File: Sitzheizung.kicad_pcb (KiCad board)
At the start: 2 copper layers, 1 part, among them Q1 BUK9M9R1-40EX

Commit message: finished layout
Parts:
- added C1: 100n, Capacitor_SMD:C_0805_2012Metric_Pad1.15x1.40mm_HandSolder, F.Cu at (163.5, 102.8)
- added C2: 10u, Capacitor_THT:CP_Radial_D8.0mm_P5.00mm, F.Cu at (146.5, 113.8)
- added C3: 100n, Capacitor_SMD:C_0805_2012Metric_Pad1.15x1.40mm_HandSolder, F.Cu at (156.1, 97.6)
- added C4: 1u, Capacitor_THT:CP_Radial_D8.0mm_P5.00mm, F.Cu at (156.2, 109.8)
- added D1: D, Diode_SMD:D_MiniMELF, F.Cu at (145.2, 97.7)
- added D2: LED, LED_SMD:LED_0805_2012Metric_Pad0.98x1.40mm_HandSolder, F.Cu at (154.7, 92.8)
- added J1: Conn_01x06_Male, Connector_TE-Connectivity:TE_MQS_936287-2_1x06_P2.54mm_Horizontal, F.Cu at (139.9, 98.0)
- added R1: 650R, Resistor_SMD:R_0805_2012Metric_Pad1.15x1.40mm_HandSolder, F.Cu at (157.2, 92.8)
- added R2: R, Resistor_SMD:R_0805_2012Metric_Pad1.15x1.40mm_HandSolder, F.Cu at (151.5, 97.6)
- added R3: 1k, Resistor_SMD:R_0805_2012Metric_Pad1.15x1.40mm_HandSolder, F.Cu at (150.3, 109.0)
- added R4: 15k, Resistor_SMD:R_0805_2012Metric_Pad1.15x1.40mm_HandSolder, F.Cu at (149.7, 102.9)
- added R5: 1k8, Resistor_SMD:R_0805_2012Metric_Pad1.15x1.40mm_HandSolder, F.Cu at (160.9, 97.7)
- added R6: 1k, Resistor_SMD:R_0805_2012Metric_Pad1.15x1.40mm_HandSolder, F.Cu at (161.8, 108.5)
- added RV1: 15k, Potentiometer_THT:Potentiometer_Bourns_3386X_Horizontal, F.Cu at (145.2, 94.3)
- added U1: TL494, Package_SO:SOIC-16_3.9x9.9mm_P1.27mm, F.Cu at (156.6, 102.8)
- moved Q1 107.8 mm to (144.9, 103.8), turned to 90 degrees
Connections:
- Q1 pad 4: (no net) -> Net-(Q1-Pad4)
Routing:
- net Net-(C1-Pad1): track 0.00 -> 41.9 mm, vias 0 -> 3
- net Poti_1: track 0.00 -> 38.3 mm, vias 0 -> 2
- net KL31: track 0.00 -> 32.1 mm, vias 0 -> 7
- net Heizung+: track 0.00 -> 27.0 mm, vias 0 -> 1
- net Heizung-: track 0.00 -> 19.1 mm, vias 0 -> 7
- net Net-(R2-Pad1): track 0.00 -> 18.2 mm, vias 0 -> 2
- net Net-(R4-Pad2): track 0.00 -> 17.7 mm
- net Net-(R3-Pad1): track 0.00 -> 6.64 mm
- net Net-(R3-Pad2): track 0.00 -> 5.81 mm
- net Net-(C4-Pad1): track 0.00 -> 4.64 mm
- net Net-(Q1-Pad4): track 0.00 -> 4.62 mm
- net Net-(R6-Pad1): track 0.00 -> 4.29 mm
- net Net-(D2-Pad2): track 0.00 -> 2.61 mm
- added copper zone on B.Cu, net Heizung-
- added copper zone on F.Cu, net Heizung-
- added copper zone on B.Cu, net KL31
- added copper zone on F.Cu, net KL31
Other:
- board outline added: 34 x 34 mm
- net class Default: clearance 0.2 -> 0.15
- rule trace_clearance: 0.2 -> 0.15
- rule trace_min: 0.2 -> 0.15
- board text added: "Auxilary Heater"
- board text added: "v1.0"

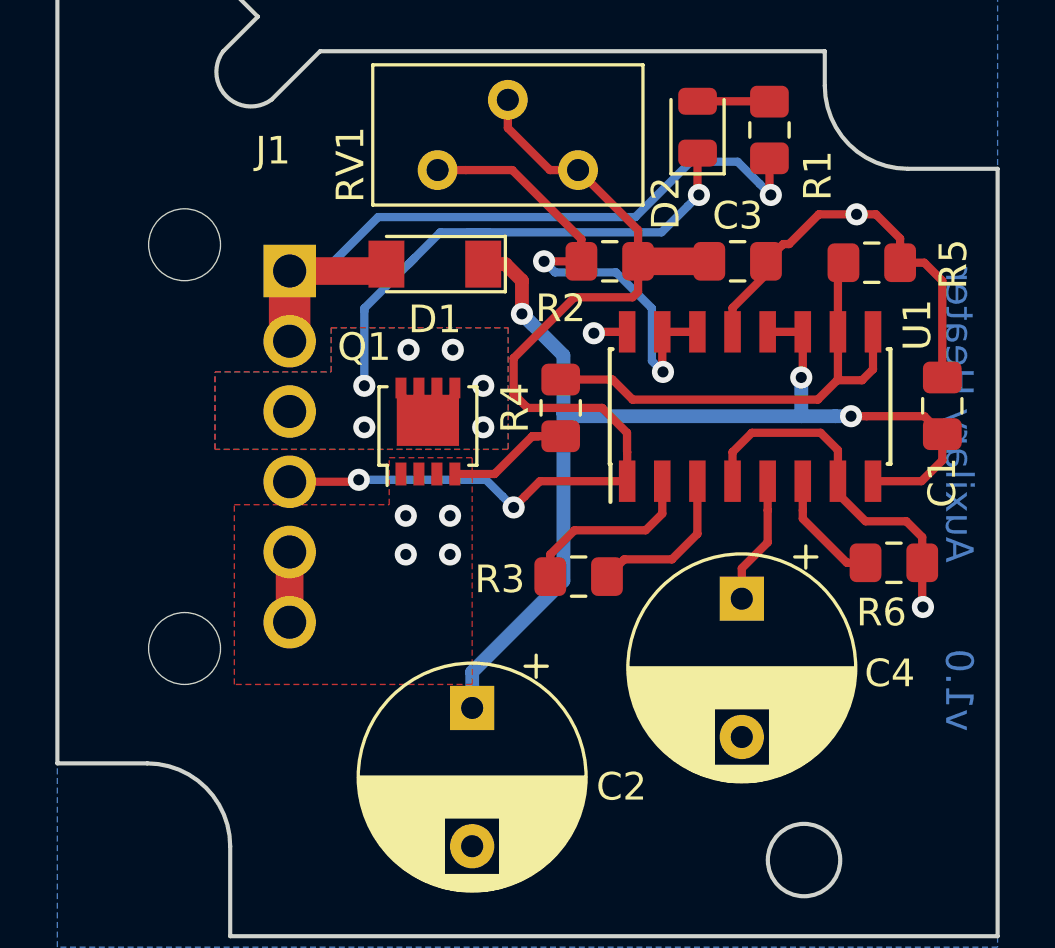
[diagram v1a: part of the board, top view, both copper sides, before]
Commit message: changed potentiometer
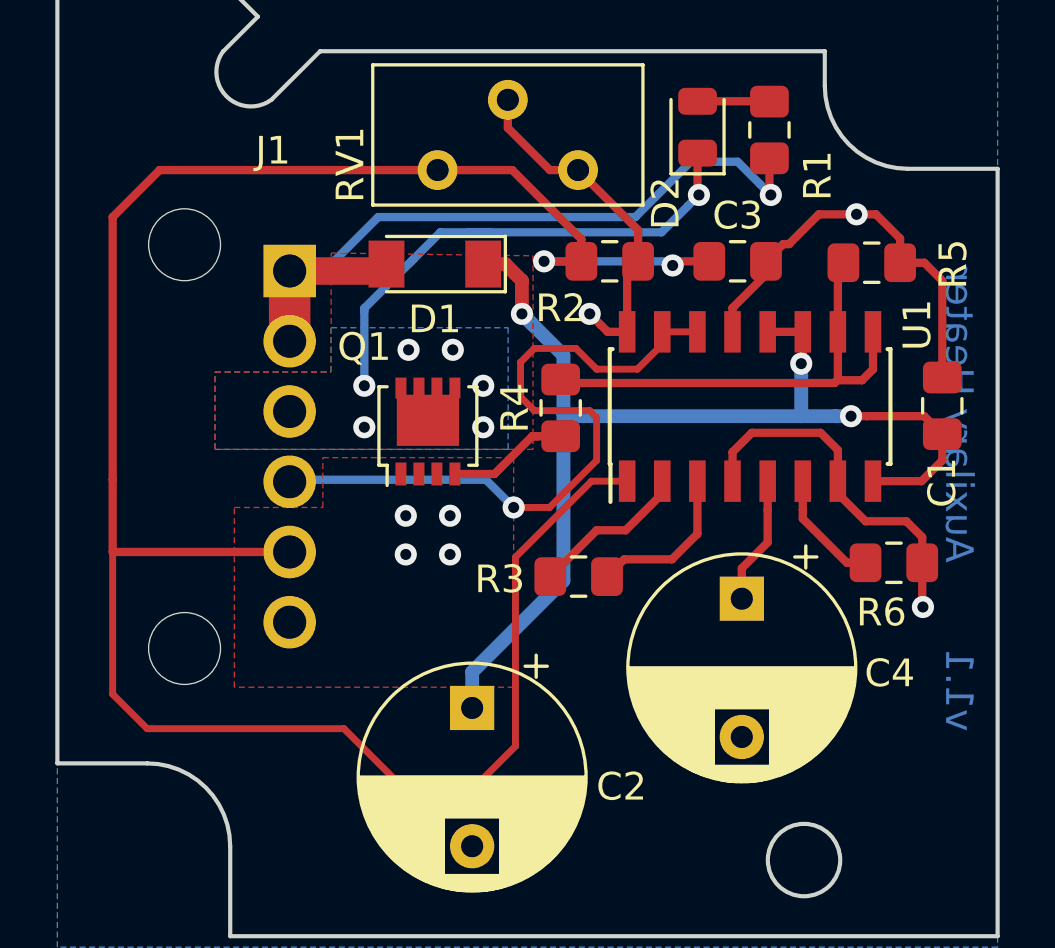
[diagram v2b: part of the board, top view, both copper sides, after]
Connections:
- C3 pad 1: Poti_1 -> Poti_2
- J1 pad 5: KL31 -> Poti_2
- R2 pad 1: Net-(R2-Pad1) -> Poti_2
- R2 pad 2: Poti_1 -> KL31
- RV1 pad 1: Net-(R2-Pad1) -> Poti_2
- RV1 pad 2: Poti_1 -> KL31
- RV1 pad 3: Poti_1 -> KL31
- U1 pad 1: Poti_1 -> Poti_2
- U1 pad 14: Net-(R2-Pad1) -> Poti_1
- U1 pad 15: Net-(R2-Pad1) -> Poti_1
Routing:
- net Poti_2: track 0.00 -> 81.5 mm, vias 0 -> 2
- net Net-(R2-Pad1): track 18.2 -> 0.00 mm, vias 2 -> 0
- net Poti_1: track 38.3 -> 25.9 mm, vias 2 -> 1
- net KL31: track 32.1 -> 41.1 mm
- net Net-(R3-Pad1): track 6.64 -> 5.74 mm
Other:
- rule pad_to_mask_clearance: 0.2 -> 0.05
- board text added: "v1.1"
- board text removed: "v1.0"

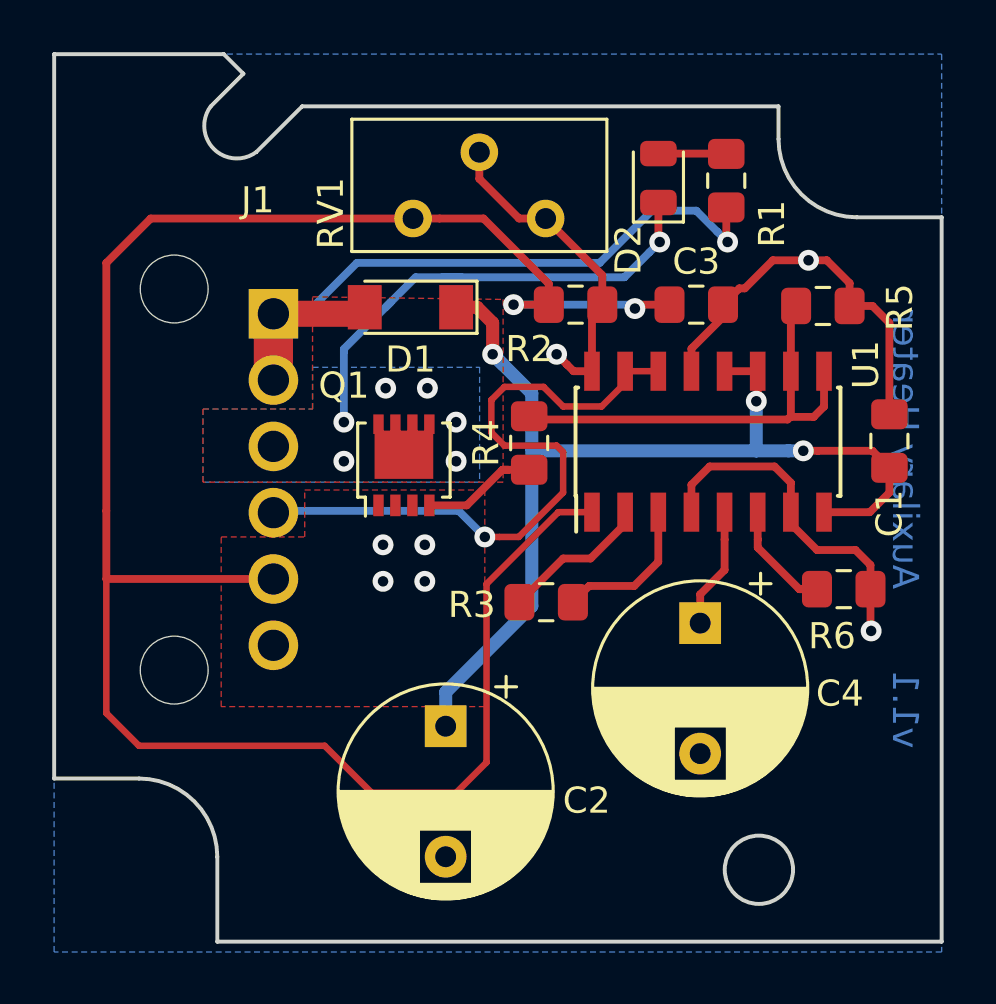
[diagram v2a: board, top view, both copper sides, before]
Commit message: added LDO
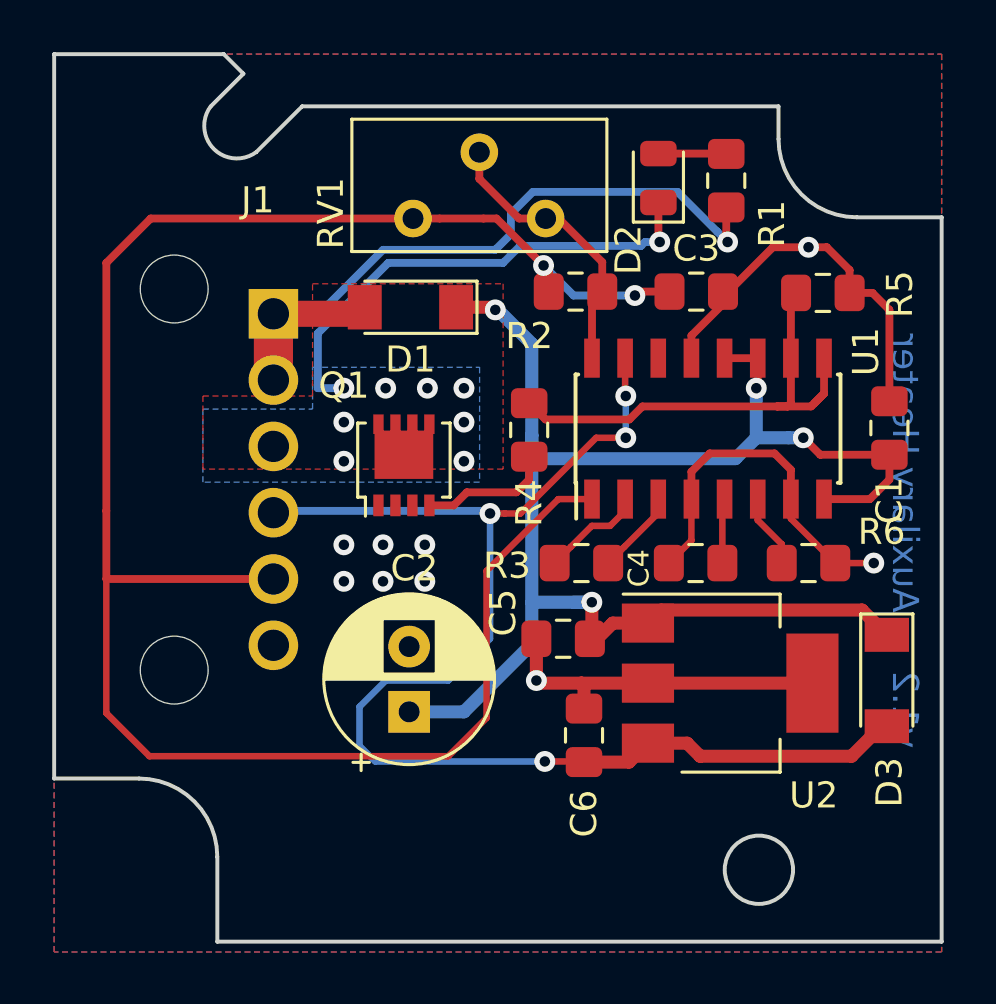
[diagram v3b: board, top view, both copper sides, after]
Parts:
- added C5: 330n, Capacitor_SMD:C_0805_2012Metric_Pad1.15x1.40mm_HandSolder, F.Cu at (151.0, 110.4)
- added C6: 100n, Capacitor_SMD:C_0805_2012Metric_Pad1.15x1.40mm_HandSolder, F.Cu at (151.8, 114.1)
- added D3: LL4148, Diode_SMD:D_MiniMELF, F.Cu at (163.4, 112.0)
- added U2: uA7805, Package_TO_SOT_SMD:SOT-223-3_TabPin2, F.Cu at (157.4, 112.1)
- C2: footprint Capacitor_THT:CP_Radial_D8.0mm_P5.00mm -> Capacitor_THT:CP_Radial_D6.3mm_P2.50mm
- C4: footprint Capacitor_THT:CP_Radial_D8.0mm_P5.00mm -> Capacitor_SMD:C_0805_2012Metric_Pad1.15x1.40mm_HandSolder
- D1: value D -> LL4148
- R1: value 650R -> 1k
- RV1: value 15k -> 200R
- moved C4 2.31 mm to (156.1, 107.5), turned to 180 degrees
- moved R3 2.02 mm to (151.7, 107.5)
- moved R6 1.68 mm to (160.4, 107.5)
- moved C2 1.50 mm to (145.1, 113.2), turned to 90 degrees
- moved C1 0.50 mm to (163.5, 102.3)
- moved C3 0.50 mm to (156.1, 97.1)
- moved R2 0.50 mm to (151.5, 97.1)
- moved R4 0.50 mm to (149.7, 102.4)
- moved R5 0.50 mm to (160.9, 97.2)
- moved U1 0.50 mm to (156.6, 102.3)
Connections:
- net Net-(C1-Pad1) renamed /VIN
- U1 pad 14: Poti_1 -> (no net)
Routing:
- net Poti_1: track 25.9 -> 51.7 mm, vias 1 -> 4
- net /VIN: track 41.9 -> 60.7 mm, vias 3 -> 4
- net KL31: track 41.1 -> 53.2 mm, vias 7 -> 9
- net Poti_2: track 81.5 -> 77.9 mm
- net Net-(R3-Pad2): track 5.81 -> 3.25 mm
- net Net-(C4-Pad1): track 4.64 -> 2.49 mm
- net Net-(R3-Pad1): track 5.74 -> 3.98 mm
- net Net-(R4-Pad2): track 17.3 -> 18.8 mm
- net Net-(R6-Pad1): track 4.29 -> 2.83 mm
- net Heizung+: track 27.0 -> 28.1 mm
- net Heizung-: track 19.1 -> 19.2 mm, vias 7 -> 9
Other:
- board text added: "v1.2"
- board text removed: "v1.1"
